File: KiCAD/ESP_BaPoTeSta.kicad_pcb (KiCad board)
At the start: 2 copper layers, 39.4 x 49.5 mm, 36 parts, among them M3 MountingHole_3.2mm_M3_ISO7380, P1 ProgHdr, P10 CONN_01X04, P13 CONN_01X03, P15 CONN_01X04, P2 Battery, P3 MicroUSB, P4 Flash, P5 Conf, P9 CONN_01X04, Q1 IRLML6302, U1 MCP1700-330, U2 ESP-12, U3 MCP73831-2-OT

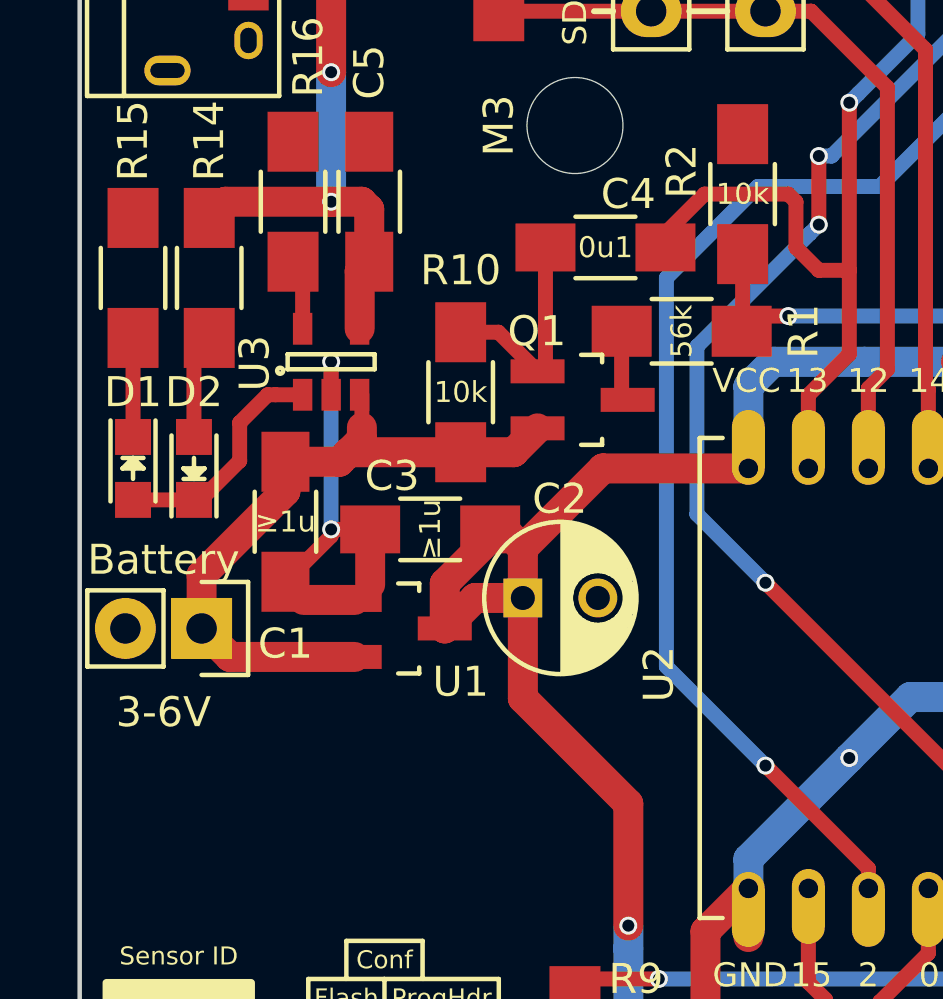
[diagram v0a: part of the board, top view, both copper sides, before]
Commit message: ENH: Use SMD capacitor as C2
fixes #24
fixes #30
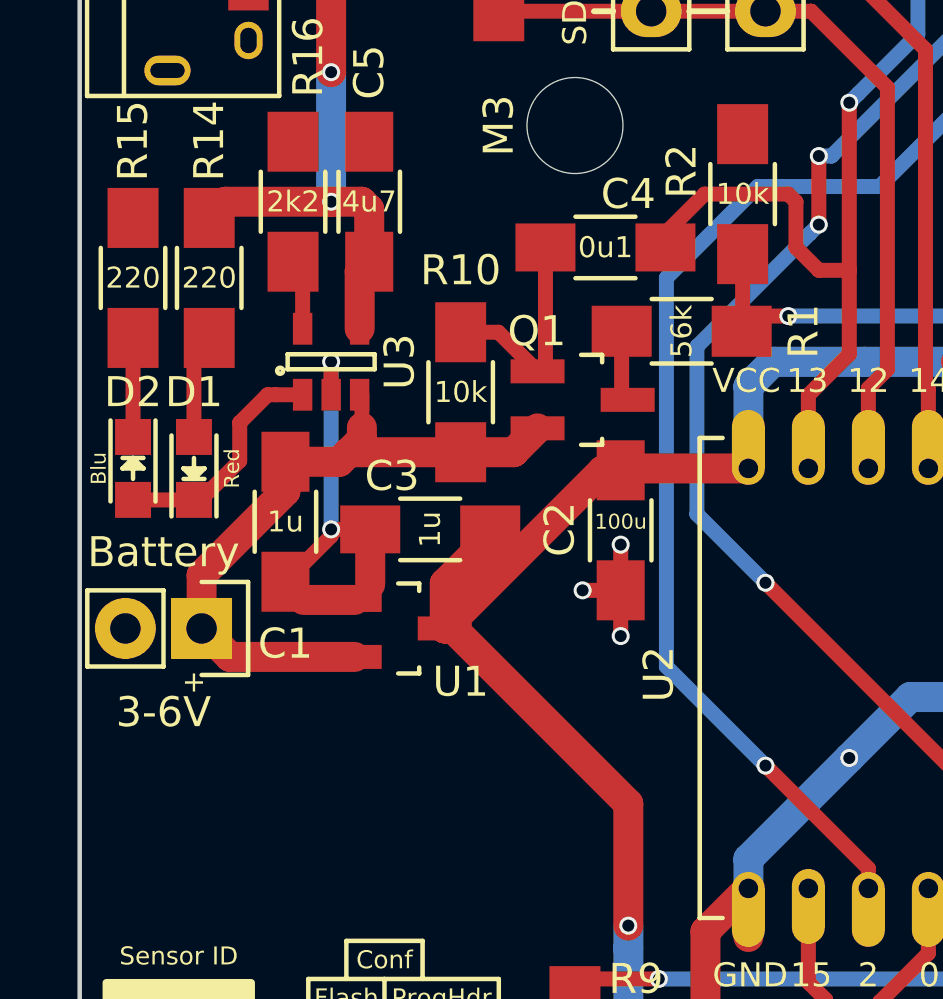
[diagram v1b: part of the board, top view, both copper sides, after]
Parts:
- C1, C3: value ≥1u -> 1u
- C2: value ≥10u -> 100u; footprint Capacitors_ThroughHole:C_Radial_D5_L11_P2.5 -> Capacitors_SMD:C_1206_HandSoldering
- moved C2 3.96 mm to (141.2, 93.5), turned to 270 degrees
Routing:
- net GND: track 46.5 -> 50.8 mm, vias 4 -> 7
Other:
- board text added: "+"

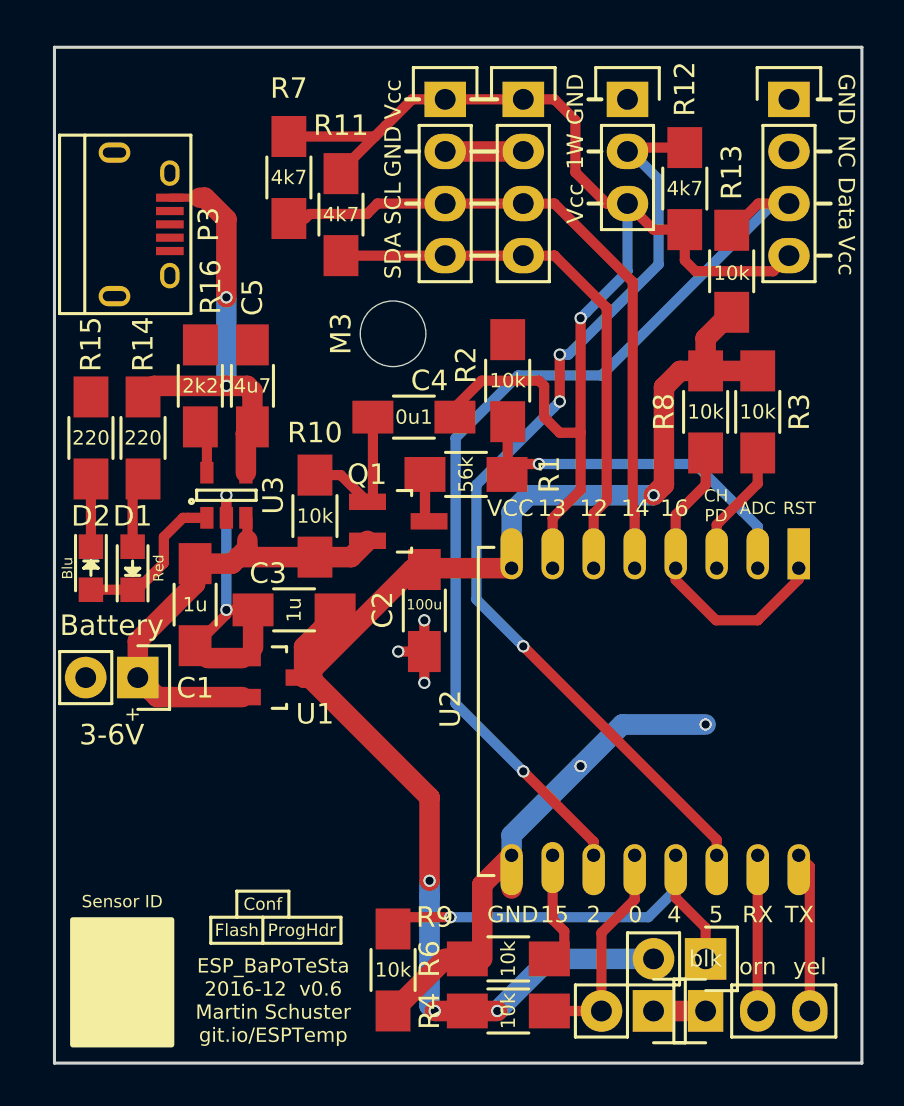
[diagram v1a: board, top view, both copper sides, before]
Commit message: ENH: PCB: Prevent undervoltage
If the undervoltage-sensor NCP300 senses too low a battery voltage,
it will tie its output to GND, thus switching off the BSS806N
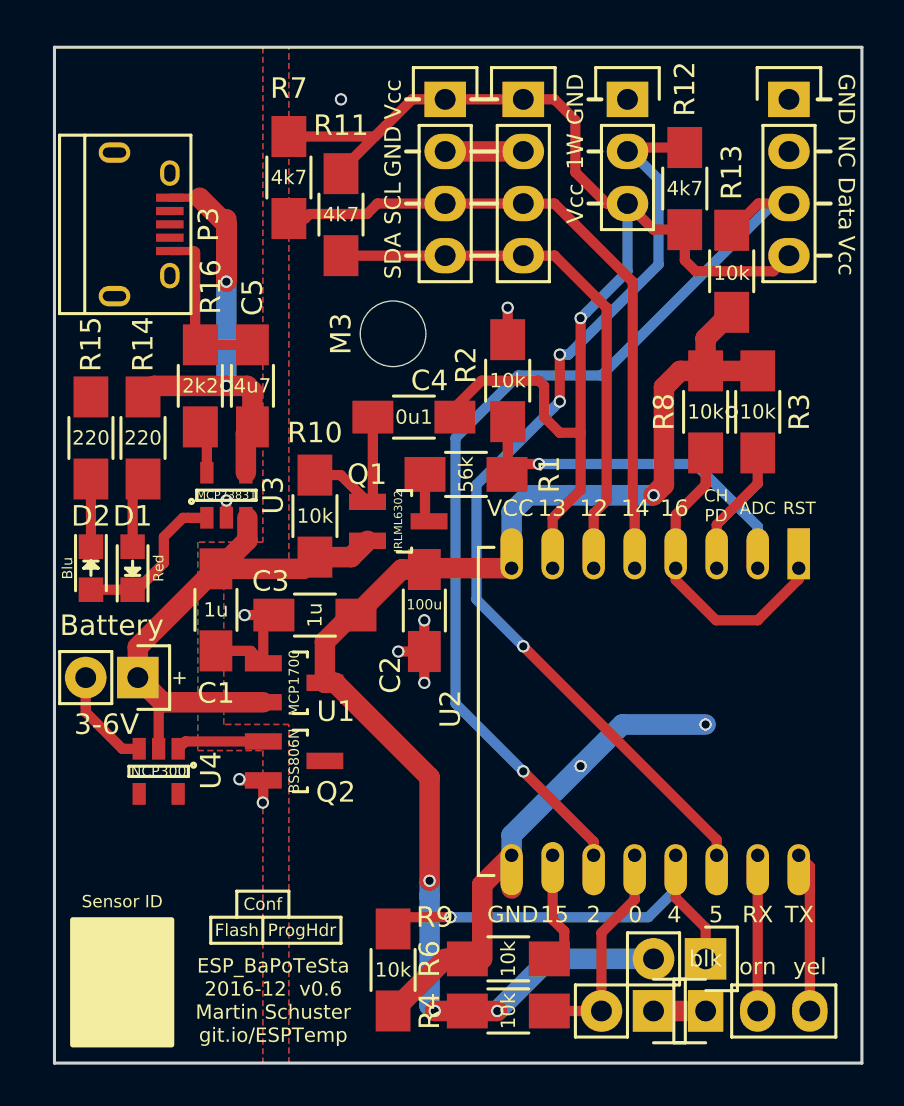
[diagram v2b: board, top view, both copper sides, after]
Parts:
- added Q2: BSS806N, TO_SOT_Packages_SMD:SOT-23_Handsoldering, F.Cu at (134.9, 100.8)
- added U4: NCP300, TO_SOT_Packages_SMD:SOT-23-5, F.Cu at (128.3, 101.3)
- U1: value MCP1700-330 -> MCP1700
- U3: value MCP73831-2-OT -> MCP73831
- moved C3 1.05 mm to (135.9, 93.7)
- moved U1 1.05 mm to (134.9, 97.0)
- moved C1 1.05 mm to (131.1, 93.5)
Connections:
- C5 pad 2: GND -> GNDPWR
- P2 pad 2: GND -> GNDPWR
- P3 pad 5: GND -> GNDPWR
- P3 pad 6: GND -> GNDPWR
- R15 pad 2: GND -> GNDPWR
- R16 pad 2: GND -> GNDPWR
- U3 pad 2: GND -> GNDPWR
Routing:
- net GNDPWR: track 0.00 -> 16.6 mm, vias 0 -> 3
- net GND: track 50.8 -> 43.4 mm
- net VCC: track 73.0 -> 67.2 mm
- net +BATT: track 23.2 -> 28.5 mm
- net /S_UV: track 0.00 -> 4.30 mm
- net /Vin: track 21.1 -> 24.0 mm
- net (no net): vias 0 -> 2
- added copper zone on B.Cu, net GNDPWR
- added copper zone on F.Cu, net GNDPWR

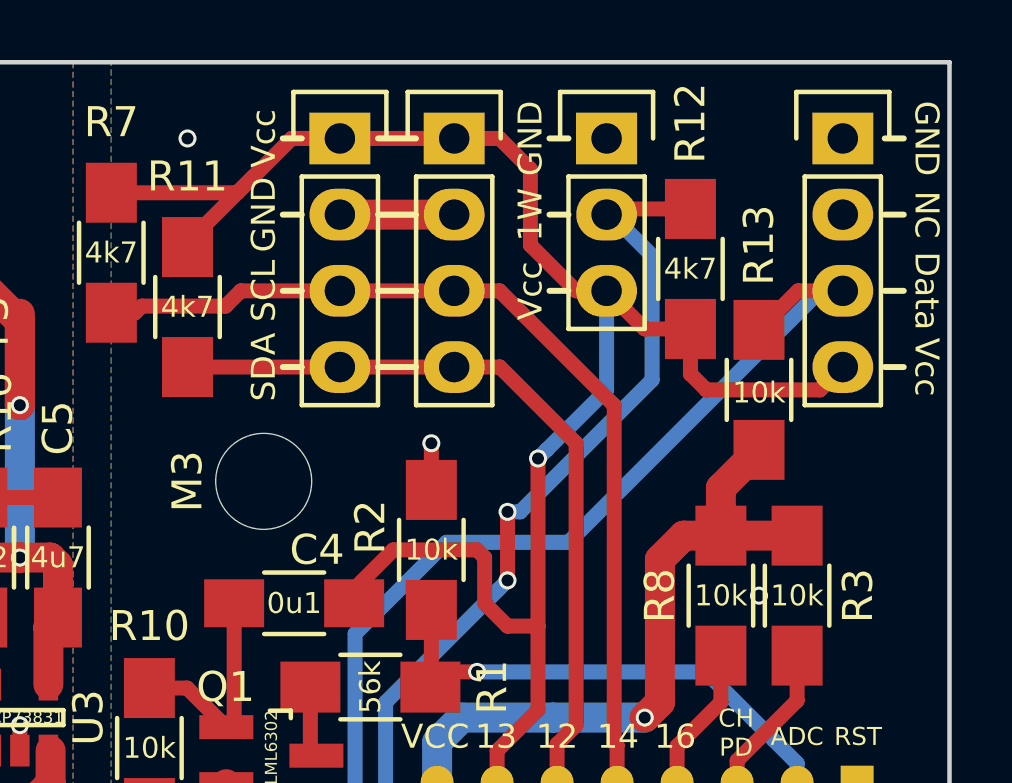
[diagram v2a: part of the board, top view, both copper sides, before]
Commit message: ENH: PCB: Thermal relief for SMD GND pads
fixes #22
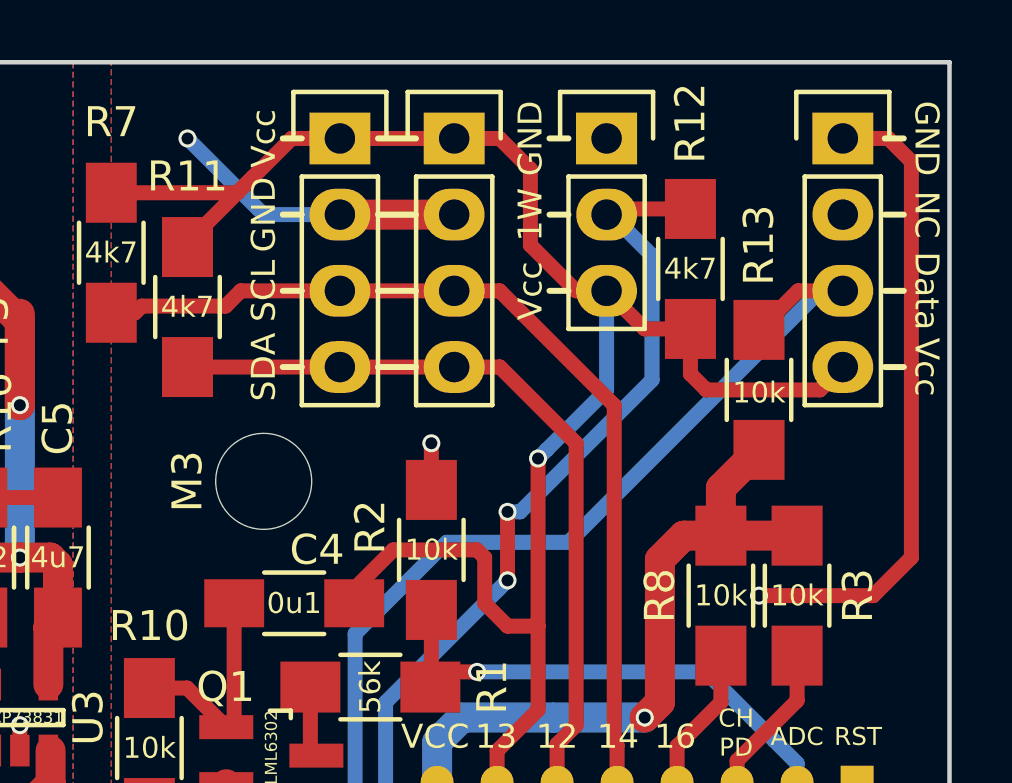
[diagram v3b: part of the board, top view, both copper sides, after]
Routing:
- net GND: track 43.4 -> 70.9 mm, vias 7 -> 9
- net (no net): vias 2 -> 0
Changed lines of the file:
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@@
     (links 81)
     (no_connects 0)
-    (area 123.114999 65.964999 162.635001 115.645001)
+    (area 122.728999 63.042619 168.455001 115.645001)
     (thickness 1.6)
     (drawings 101)
-    (tracks 249)
+    (tracks 256)
     (zones 0)
     (modules 38)
@@
   (gr_line (start 123.19 115.57) (end 123.19 66.04) (angle 90) (layer Edge.Cuts) (width 0.15))
   (gr_line (start 162.56 66.04) (end 162.56 115.57) (angle 90) (layer Edge.Cuts) (width 0.15))
-  (via (at 156.21 83.82) (size 0.6) (drill 0.4) (layers F.Cu B.Cu) (net 0))
-  (via (at 137.16 68.58) (size 0.6) (drill 0.4) (layers F.Cu B.Cu) (net 0))
   (segment (start 131.064 91.472) (end 135.318 91.472) (width 1) (layer F.Cu) (net 1))
   (segment (start 135.318 91.472) (end 135.89 90.9) (width 1) (layer F.Cu) (net 1))
@@
   (segment (start 135.89 90.9) (end 137.65686 90.9) (width 1) (layer F.Cu) (net 1))
   (segment (start 137.65686 90.9) (end 138.45286 90.104) (width 1) (layer F.Cu) (net 1))
+  (segment (start 161.29 82.55) (end 160.02 83.82) (width 0.5) (layer F.Cu) (net 2))
+  (segment (start 160.02 83.82) (end 156.21 83.82) (width 0.5) (layer F.Cu) (net 2))
+  (via (at 156.21 83.82) (size 0.6) (drill 0.4) (layers F.Cu B.Cu) (net 2))
+  (segment (start 161.29 69.35) (end 161.29 82.55) (width 0.5) (layer F.Cu) (net 2))
+  (segment (start 159.004 68.58) (end 160.52 68.58) (width 0.5) (layer F.Cu) (net 2))
+  (segment (start 160.52 68.58) (end 161.29 69.35) (width 0.5) (layer F.Cu) (net 2))
+  (segment (start 142.24 71.12) (end 139.7 71.12) (width 0.5) (layer B.Cu) (net 2))
+  (segment (start 139.7 71.12) (end 137.16 68.58) (width 0.5) (layer B.Cu) (net 2))
+  (via (at 137.16 68.58) (size 0.6) (drill 0.4) (layers F.Cu B.Cu) (net 2))
   (segment (start 133.89 93.726) (end 132.461 93.726) (width 0.5) (layer F.Cu) (net 2))
   (via (at 132.461 93.726) (size 0.6) (drill 0.4) (layers F.Cu B.Cu) (net 2))
@@
   (zone (net 2) (net_name GND) (layer F.Cu) (hatch edge 0.508)
     (priority 1)
-    (connect_pads thru_hole_only (clearance 0.508))
+    (connect_pads (clearance 0.508))
     (min_thickness 0.254)
     (fill yes (arc_segments 16) (thermal_gap 0.508) (thermal_bridge_width 0.508))

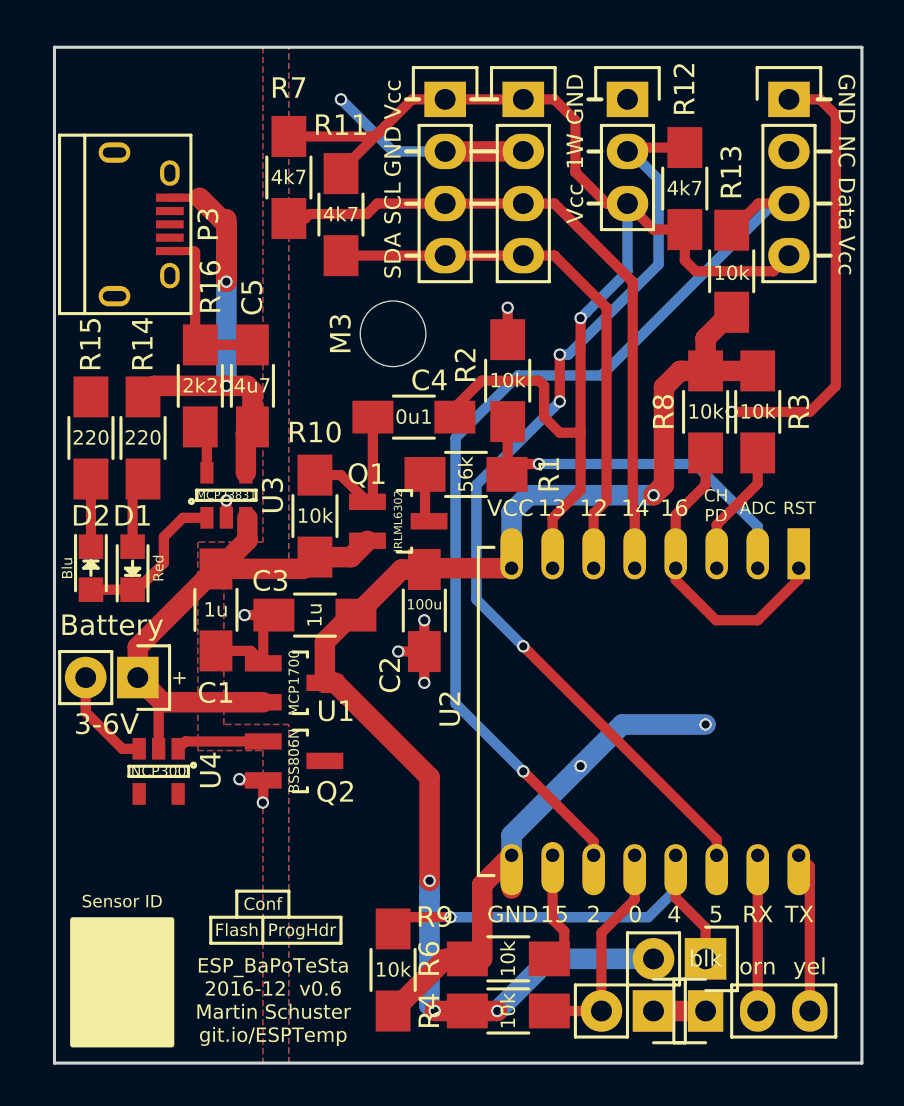
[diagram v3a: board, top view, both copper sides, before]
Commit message: ENH: PCB: Most traces are now 0.5mm
0.5mm (20mill) are more than enough for the low currents (500mA)

Only the "main" trace (USB+ to MCP73831 to battery to MCP1700 to ESP)
is still 1mm (40mill).

GND is transferred via the copper planes.

fixes #31
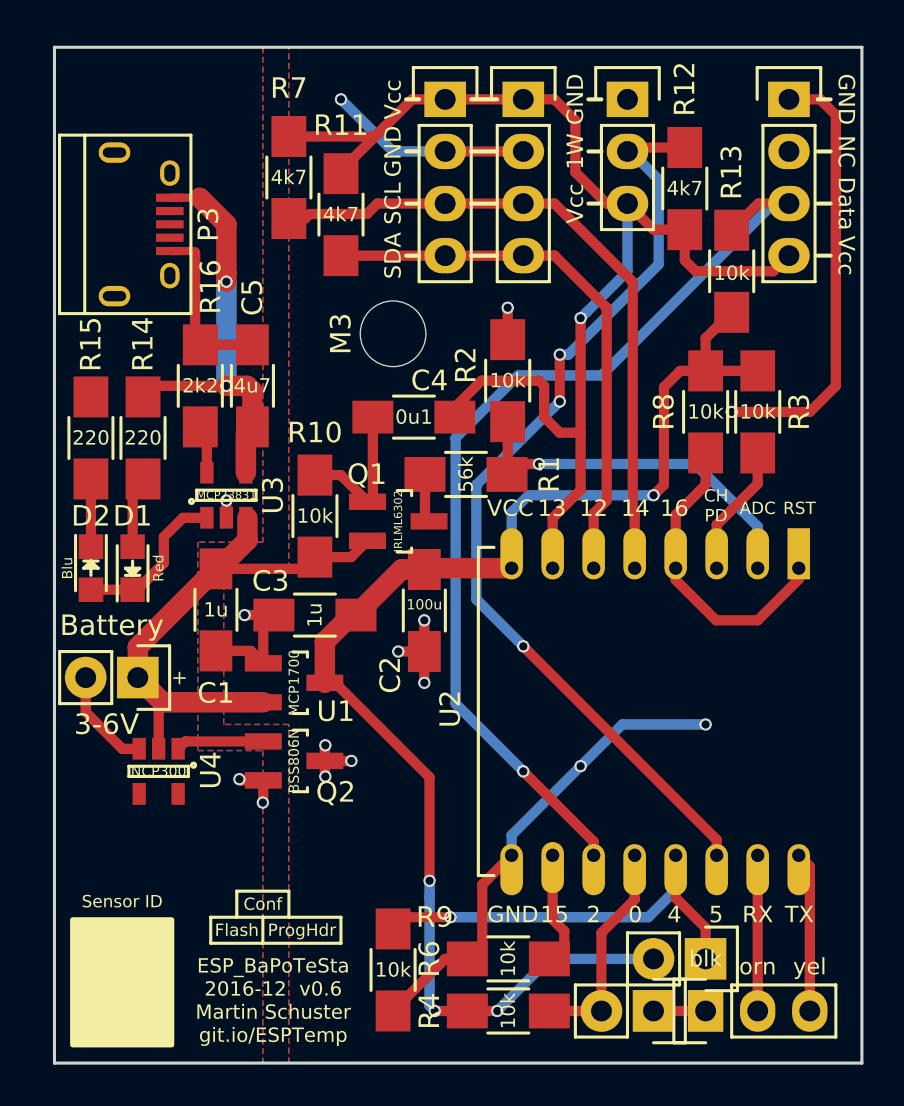
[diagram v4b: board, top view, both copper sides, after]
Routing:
- net /Vin: track 24.0 -> 20.9 mm
- net GND: track 70.9 -> 73.8 mm, vias 9 -> 12
- net +BATT: track 28.5 -> 27.1 mm
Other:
- net class Power: trace_width 1 -> 0.5

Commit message: WIP: PCB: Add ATmega328P-AU
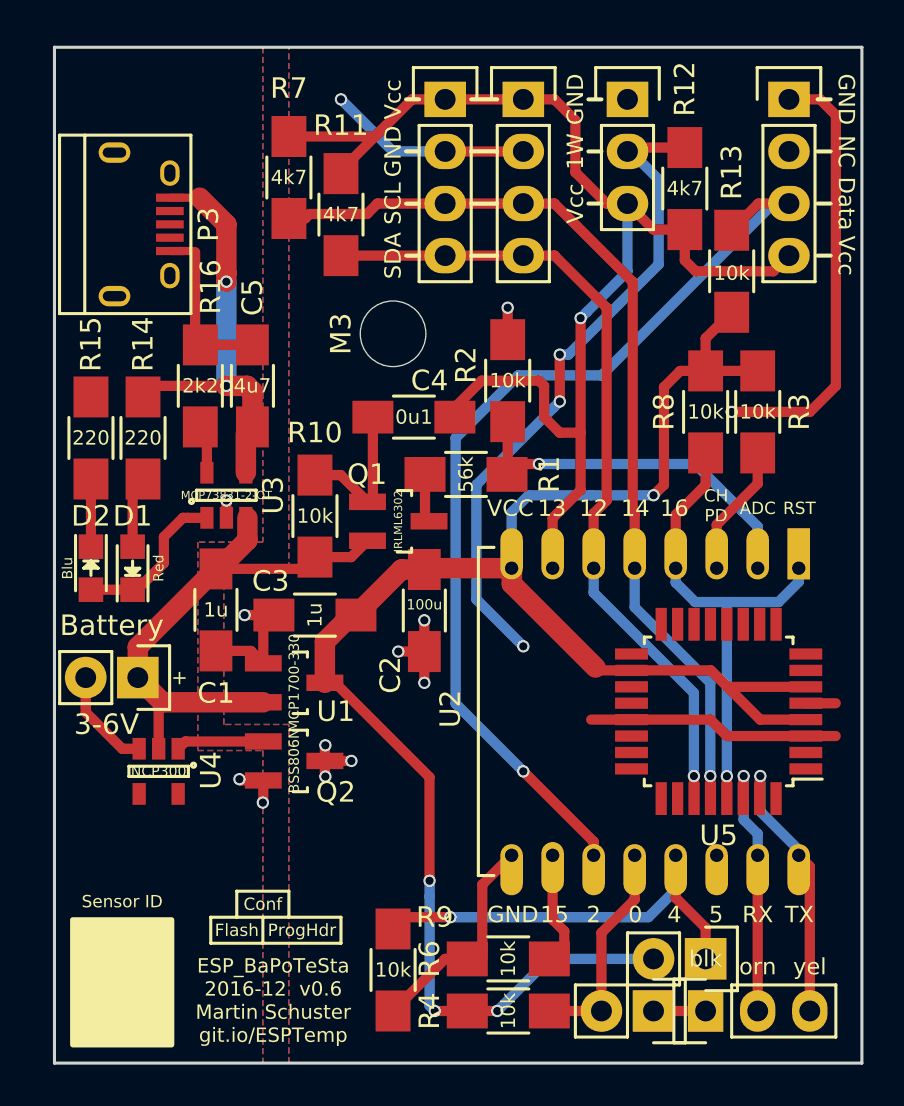
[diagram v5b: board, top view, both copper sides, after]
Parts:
- added U5: ATMEGA328P-A, Housings_QFP:TQFP-32_7x7mm_Pitch0.8mm, F.Cu at (155.6, 98.4)
- U1: value MCP1700 -> MCP1700-330
- U3: value MCP73831 -> MCP73831-2-OT
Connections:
- net /RST renamed RST
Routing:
- net VCC: track 67.2 -> 89.0 mm
- net 1Wire: track 46.7 -> 32.6 mm
- net SDA: track 27.0 -> 40.2 mm, vias 0 -> 1
- net SCL: track 32.6 -> 45.4 mm, vias 0 -> 1
- net RST: track 15.0 -> 24.0 mm, vias 0 -> 1
- net TXD: track 7.81 -> 13.6 mm, vias 0 -> 1
- net RXD: track 7.59 -> 12.8 mm, vias 0 -> 1
- net GND: track 73.8 -> 74.8 mm, vias 12 -> 10
